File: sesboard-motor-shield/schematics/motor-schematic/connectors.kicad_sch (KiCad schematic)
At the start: 2 parts, among them J3 SESBOARD_1, J4 SESBOARD_2

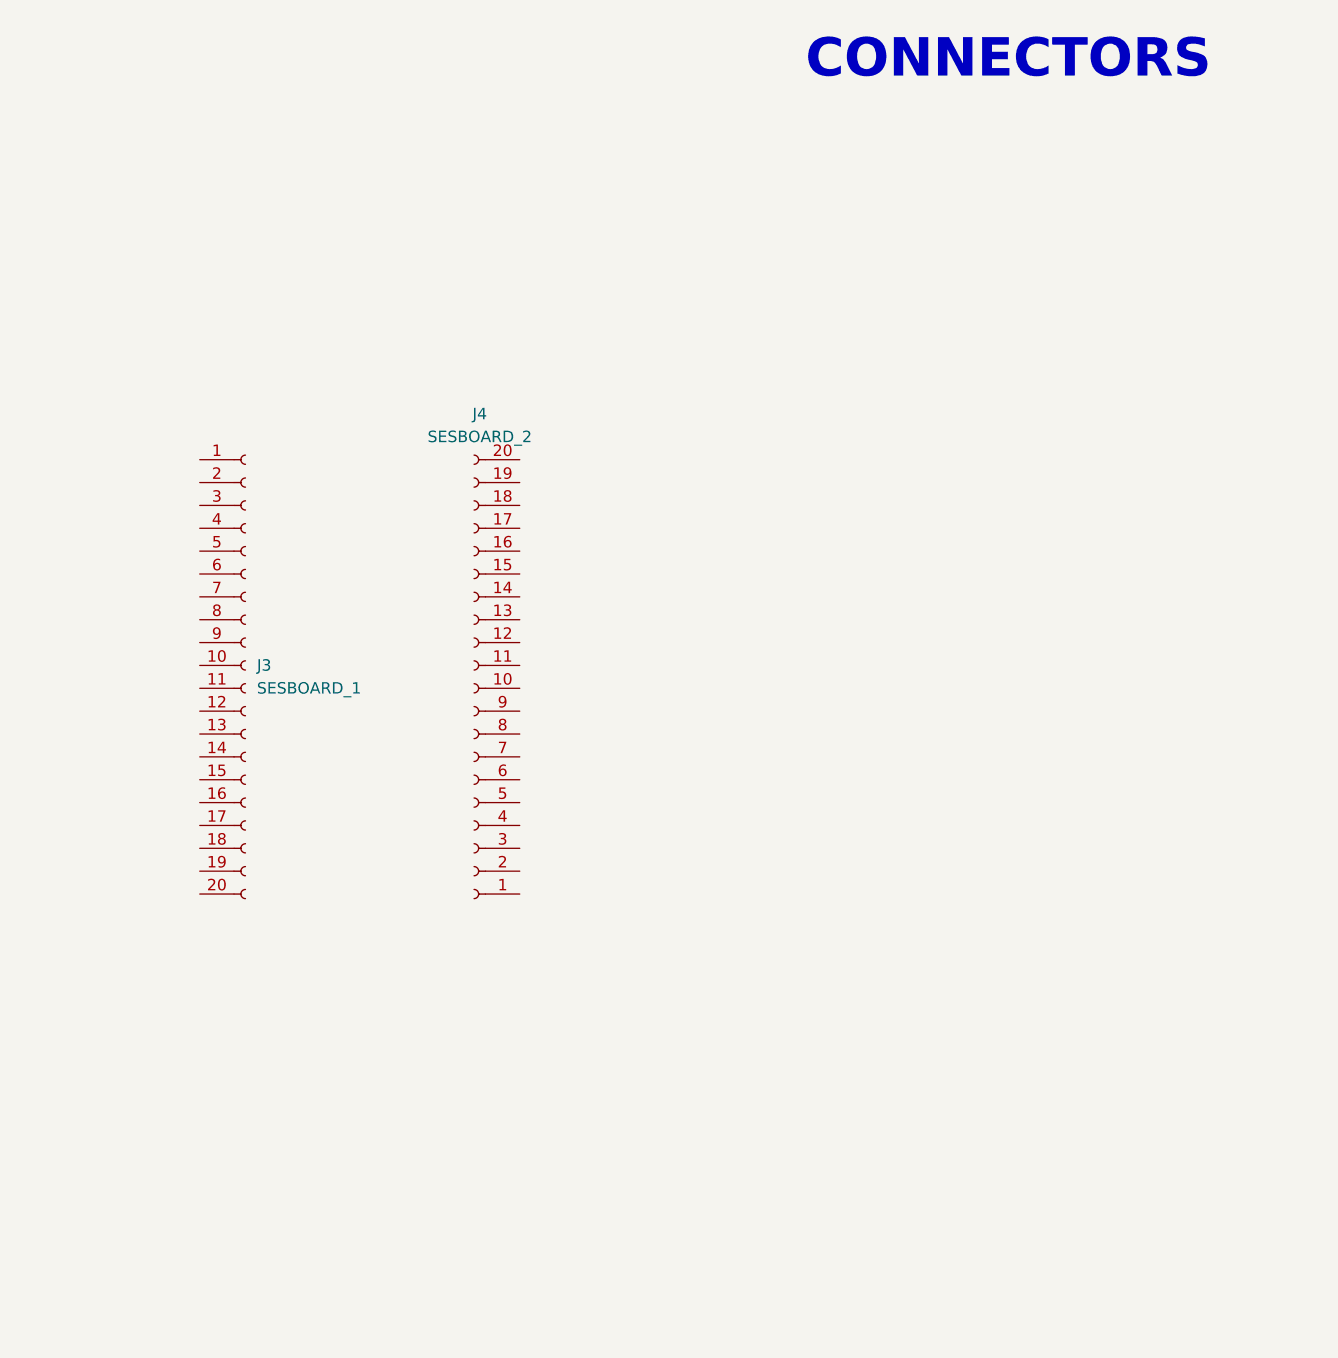
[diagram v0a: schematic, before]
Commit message: added stepper connector
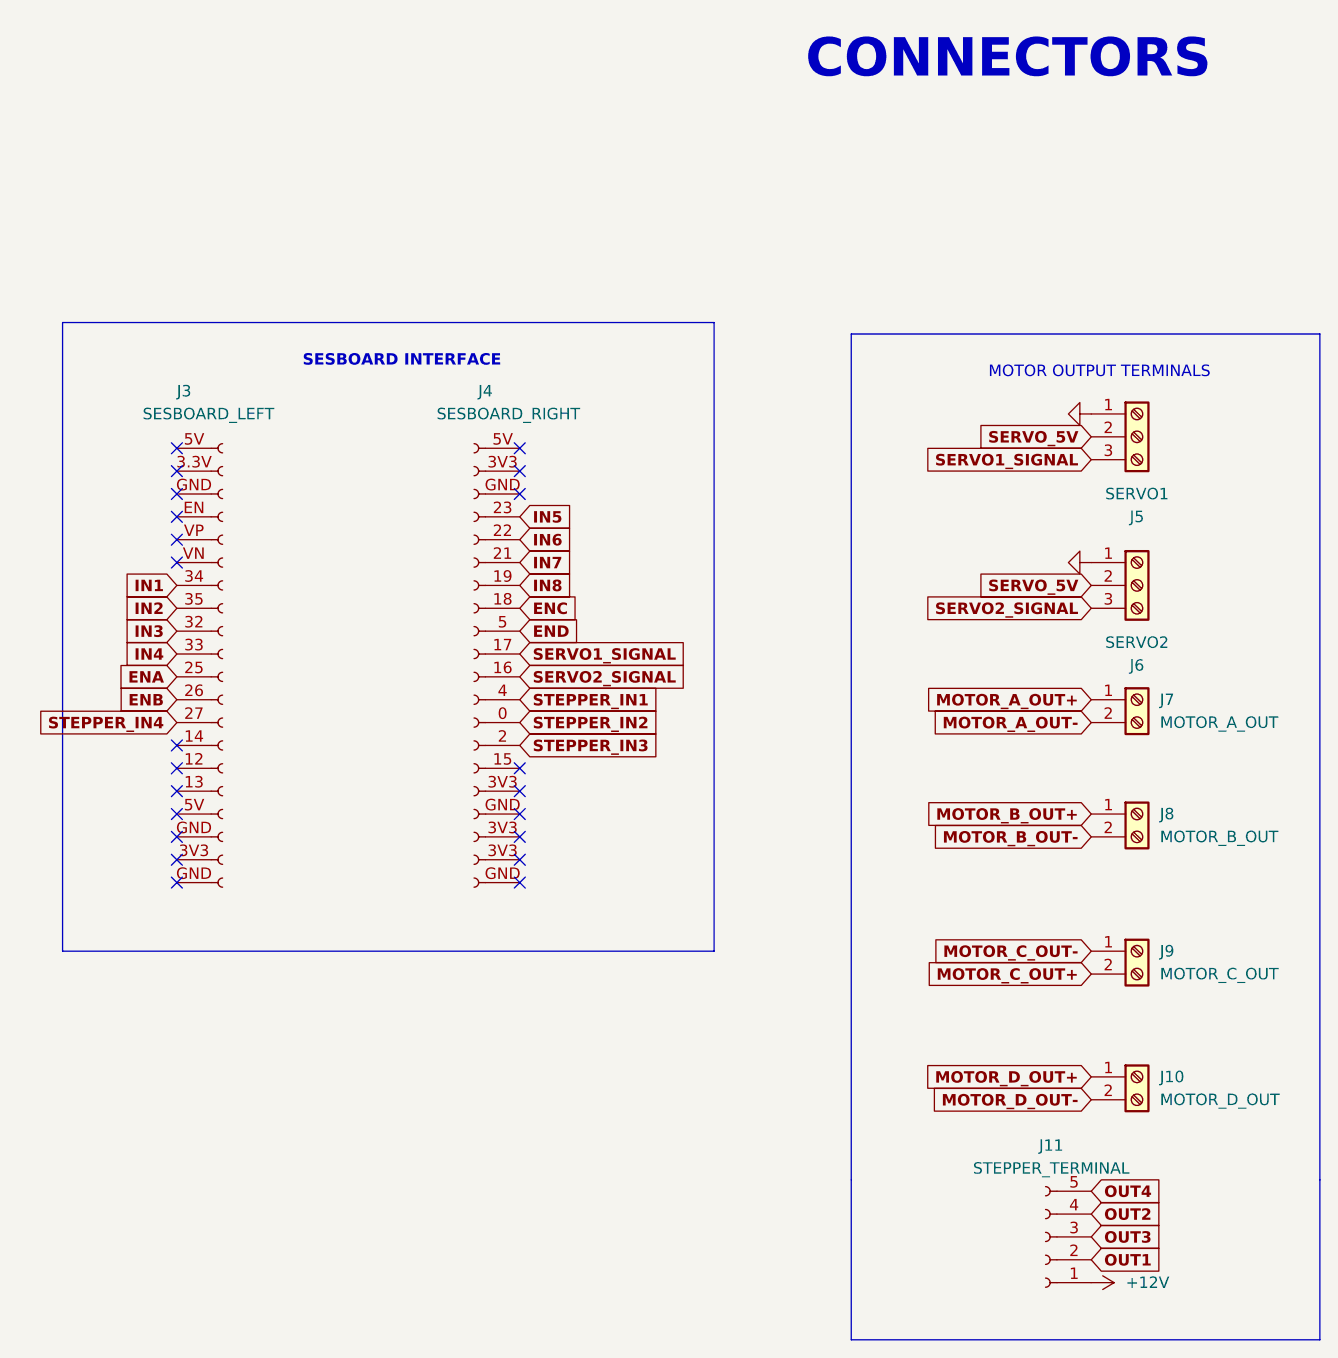
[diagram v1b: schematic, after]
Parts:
- added J10: MOTOR_D_OUT, TerminalBlock_Phoenix:TerminalBlock_Phoenix_MKDS-1,5-2_1x02_P5.00mm_Horizontal, symbol Connector:Screw_Terminal_01x02
- added J11: STEPPER_TERMINAL, Connector_PinHeader_2.54mm:PinHeader_1x05_P2.54mm_Vertical, symbol Connector:Conn_01x05_Female
- added J5: SERVO1, Connector_PinHeader_2.54mm:PinHeader_1x03_P2.54mm_Vertical, symbol Connector:Screw_Terminal_01x03
- added J6: SERVO2, Connector_PinHeader_2.54mm:PinHeader_1x03_P2.54mm_Vertical, symbol Connector:Screw_Terminal_01x03
- added J7: MOTOR_A_OUT, TerminalBlock_Phoenix:TerminalBlock_Phoenix_MKDS-1,5-2_1x02_P5.00mm_Horizontal, symbol Connector:Screw_Terminal_01x02
- added J8: MOTOR_B_OUT, TerminalBlock_Phoenix:TerminalBlock_Phoenix_MKDS-1,5-2_1x02_P5.00mm_Horizontal, symbol Connector:Screw_Terminal_01x02
- added J9: MOTOR_C_OUT, TerminalBlock_Phoenix:TerminalBlock_Phoenix_MKDS-1,5-2_1x02_P5.00mm_Horizontal, symbol Connector:Screw_Terminal_01x02
- J3: value SESBOARD_1 -> SESBOARD_LEFT
- J4: value SESBOARD_2 -> SESBOARD_RIGHT
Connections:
- net SERVO2_SIGNAL: now reaches J4.16 (11)
- net SERVO2_SIGNAL: now also J6.3 (Pin_3)
- net SERVO1_SIGNAL: now reaches J4.17 (10)
- net SERVO1_SIGNAL: now also J5.3 (Pin_3)
- net ENC: now reaches J4.18 (8)
- net IN8: now reaches J4.19 (7)
- net STEPPER_IN3: now reaches J4.2 (14)
- net STEPPER_IN1: now reaches J4.4 (12)
- net END: now reaches J4.5 (9)
- new net +12V: J11.1 (Pin_1)
- new net ENA: J3.25 (Pin_11)
- new net ENB: J3.26 (Pin_12)
- new net GND: J5.1 (Pin_1), J6.1 (Pin_1)
- new net IN1: J3.34 (7)
- new net IN2: J3.35 (8)
- new net IN3: J3.32 (9)
- new net IN4: J3.33 (Pin_10)
- new net IN5: J4.23 (4)
- new net IN6: J4.22 (5)
- new net IN7: J4.21 (6)
- new net MOTOR_A_OUT+: J7.1 (Pin_1)
- new net MOTOR_A_OUT-: J7.2 (Pin_2)
- new net MOTOR_B_OUT+: J8.1 (Pin_1)
- new net MOTOR_B_OUT-: J8.2 (Pin_2)
- new net MOTOR_C_OUT+: J9.2 (Pin_2)
- new net MOTOR_C_OUT-: J9.1 (Pin_1)
- new net MOTOR_D_OUT+: J10.1 (Pin_1)
- new net MOTOR_D_OUT-: J10.2 (Pin_2)
- new net OUT1: J11.2 (Pin_2)
- new net OUT2: J11.4 (Pin_4)
- new net OUT3: J11.3 (Pin_3)
- new net OUT4: J11.5 (Pin_5)
- new net SERVO_5V: J5.2 (Pin_2), J6.2 (Pin_2)
- new net STEPPER_IN2: J4.0 (13)
- new net STEPPER_IN4: J3.27 (Pin_13)
- no-connect marks 0 -> 22
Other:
- note added: "MOTOR OUTPUT TERMINALS"
- note added: "SESBOARD INTERFACE"
- moved on the sheet: J3

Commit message: added power toggle
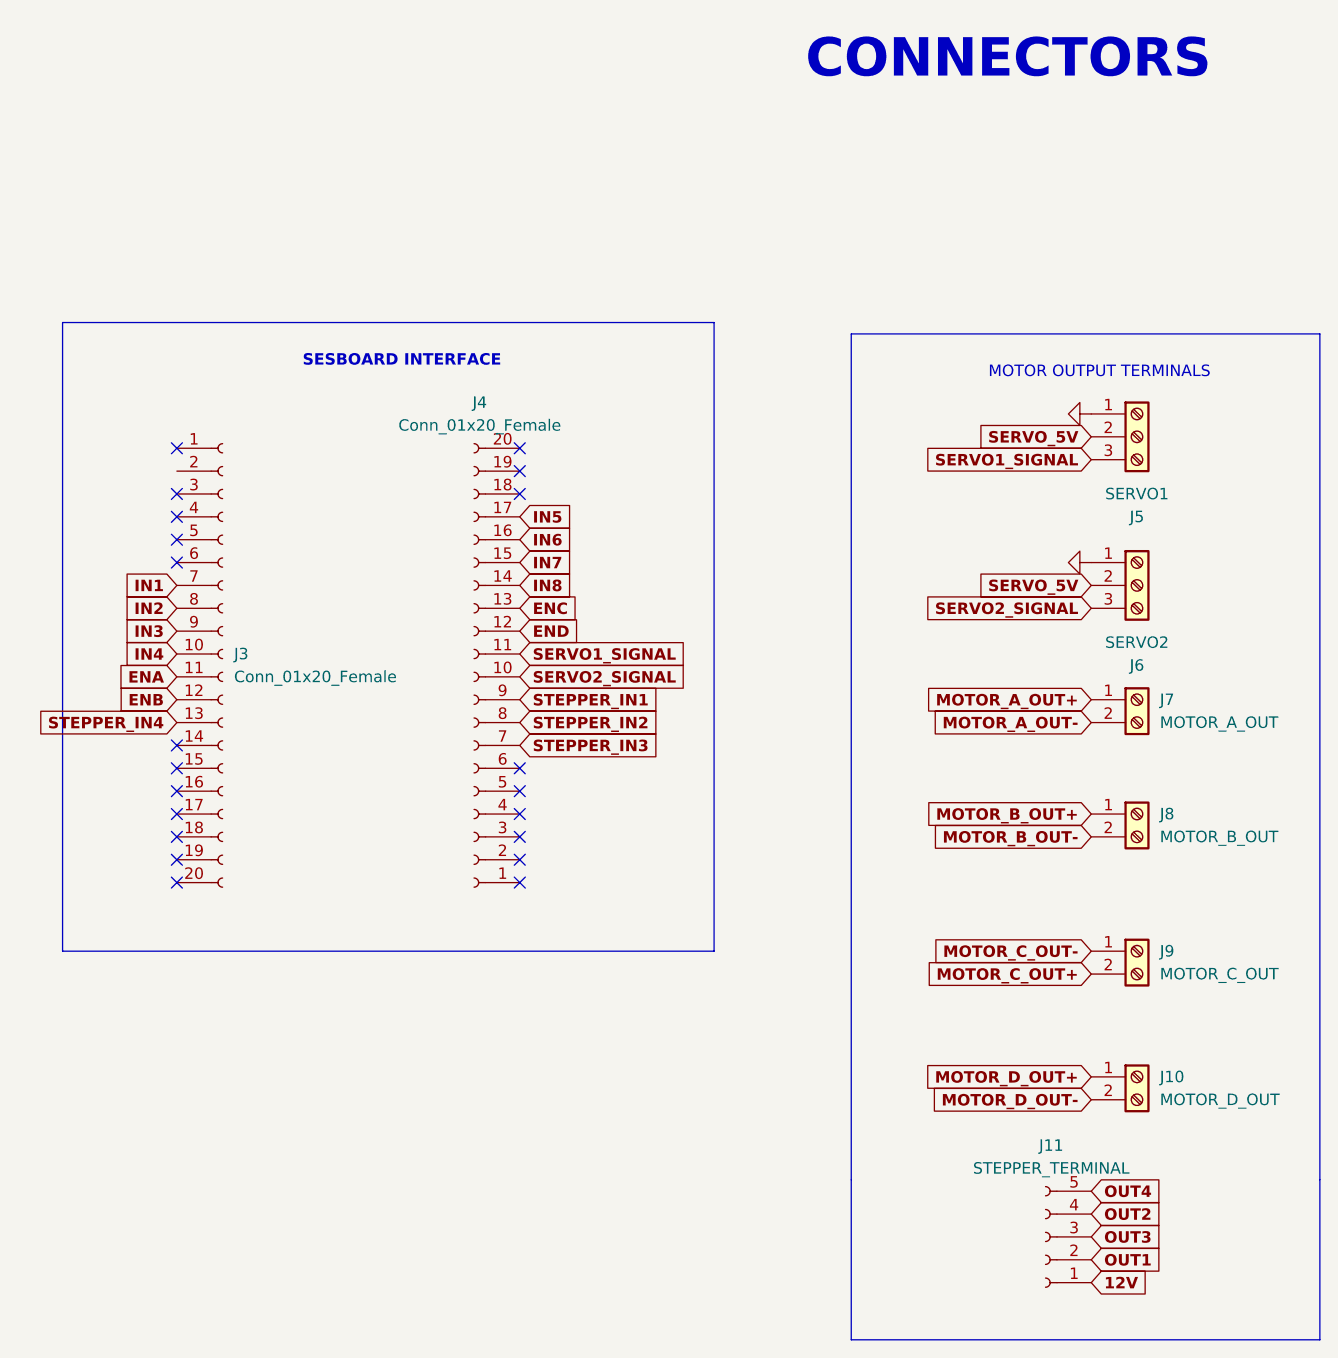
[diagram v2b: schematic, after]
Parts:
- J3: value SESBOARD_LEFT -> Conn_01x20_Female
- J4: value SESBOARD_RIGHT -> Conn_01x20_Female
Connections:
- net ENA: now also J3.11 (Pin_11); no longer J3.25 (Pin_11)
- net ENB: now also J3.12 (Pin_12); no longer J3.26 (Pin_12)
- net ENC: now also J4.13 (Pin_13); no longer J4.18 (8)
- net END: now also J4.12 (Pin_12); no longer J4.5 (9)
- net IN1: now also J3.7 (Pin_7); no longer J3.34 (7)
- net IN2: now also J3.8 (Pin_8); no longer J3.35 (8)
- net IN3: now also J3.9 (Pin_9); no longer J3.32 (9)
- net IN4: now also J3.10 (Pin_10); no longer J3.33 (Pin_10)
- net IN5: now also J4.17 (Pin_17); no longer J4.23 (4)
- net IN6: now also J4.16 (Pin_16); no longer J4.22 (5)
- net IN7: now also J4.15 (Pin_15); no longer J4.21 (6)
- net IN8: now also J4.14 (Pin_14); no longer J4.19 (7)
- net SERVO1_SIGNAL: now also J4.11 (Pin_11); no longer J4.17 (10)
- net SERVO2_SIGNAL: now also J4.10 (Pin_10); no longer J4.16 (11)
- net STEPPER_IN1: now also J4.9 (Pin_9); no longer J4.4 (12)
- net STEPPER_IN2: now also J4.8 (Pin_8); no longer J4.0 (13)
- net STEPPER_IN3: now also J4.7 (Pin_7); no longer J4.2 (14)
- net STEPPER_IN4: now also J3.13 (Pin_13); no longer J3.27 (Pin_13)
- net +12V renamed 12V
- no-connect marks 22 -> 21
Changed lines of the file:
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@@
 (kicad_sch (version 20211123) (generator eeschema)
   (paper "A4")
+  (no_connect (at 62.23 96.52))
+  (no_connect (at 62.23 99.06))
   (no_connect (at 62.23 101.6))
   (no_connect (at 100.33 99.06))
-  (no_connect (at 62.23 96.52))
-  (no_connect (at 62.23 99.06))
+  (no_connect (at 62.23 63.5))
+  (no_connect (at 62.23 73.66))
+  (no_connect (at 62.23 68.58))
+  (no_connect (at 62.23 71.12))
+  (no_connect (at 62.23 76.2))
   (no_connect (at 62.23 109.22))
   (no_connect (at 62.23 106.68))
-  (no_connect (at 100.33 101.6))
-  (no_connect (at 100.33 109.22))
-  (no_connect (at 100.33 111.76))
   (no_connect (at 62.23 104.14))
   (no_connect (at 62.23 111.76))
+  (no_connect (at 100.33 68.58))
+  (no_connect (at 100.33 66.04))
+  (no_connect (at 100.33 63.5))
+  (no_connect (at 100.33 111.76))
+  (no_connect (at 100.33 109.22))
+  (no_connect (at 100.33 101.6))
+  (no_connect (at 100.33 106.68))
   (no_connect (at 100.33 104.14))
-  (no_connect (at 100.33 106.68))
-  (no_connect (at 100.33 66.04))
-  (no_connect (at 100.33 68.58))
-  (no_connect (at 100.33 63.5))
-  (no_connect (at 62.23 63.5))
-  (no_connect (at 62.23 66.04))
-  (no_connect (at 62.23 68.58))
-  (no_connect (at 62.23 71.12))
-  (no_connect (at 62.23 73.66))
-  (no_connect (at 62.23 76.2))
   (polyline (pts (xy 189.23 162.56) (xy 189.23 144.78))
     (stroke (width 0) (type default) (color 0 0 0 0))
@@
     )
   )
+  (global_label "12V" (shape input) (at 163.83 156.21 0) (fields_autoplaced)
+    (effects (font (size 1.27 1.27) bold) (justify left))
+    (property "Intersheet References" "${INTERSHEET_REFS}" (id 0) (at 169.9411 156.083 0)
+      (effects (font (size 1.27 1.27) bold) (justify left) hide)
+    )
+  )
   (global_label "END" (shape input) (at 100.33 83.82 0) (fields_autoplaced)
     (effects (font (size 1.27 1.27) bold) (justify left))
@@
     )
   )
-  (symbol (lib_id "Connector:Screw_Terminal_01x02") (at 168.91 119.38 0) (unit 1)
-    (in_bom yes) (on_board yes) (fields_autoplaced)
-    (property "Reference" "J9" (id 0) (at 171.45 119.3799 0)
-      (effects (font (size 1.27 1.27)) (justify left))
-    )
-    (property "Value" "MOTOR_C_OUT" (id 1) (at 171.45 121.9199 0)
-      (effects (font (size 1.27 1.27)) (justify left))
-    )
-    (property "Footprint" "TerminalBlock_Phoenix:TerminalBlock_Phoenix_MKDS-1,5-2_1x02_P5.00mm_Horizontal" (id 2) (at 168.91 119.38 0)
-      (effects (font (size 1.27 1.27)) hide)
-    )
-    (property "Datasheet" "~" (id 3) (at 168.91 119.38 0)
-      (effects (font (size 1.27 1.27)) hide)
-    )
-    (pin "1")
-    (pin "2")
-  )
-  (symbol (lib_id "power:+12V") (at 163.83 156.21 270) (unit 1)
-    (in_bom yes) (on_board yes) (fields_autoplaced)
-    (property "Reference" "#PWR026" (id 0) (at 160.02 156.21 0)
-      (effects (font (size 1.27 1.27)) hide)
-    )
-    (property "Value" "+12V" (id 1) (at 167.64 156.2099 90)
-      (effects (font (size 1.27 1.27)) (justify left))
-    )
-    (property "Footprint" "" (id 2) (at 163.83 156.21 0)
-      (effects (font (size 1.27 1.27)) hide)
-    )
-    (property "Datasheet" "" (id 3) (at 163.83 156.21 0)
-      (effects (font (size 1.27 1.27)) hide)
-    )
-    (pin "1")
-  )
-  (symbol (lib_id "Connector:Conn_01x20_Female") (at 93.98 93.98 0) (unit 1)
-    (in_bom yes) (on_board yes)
-    (property "Reference" "J4" (id 0) (at 96.52 57.15 0))
-    (property "Value" "SESBOARD_RIGHT" (id 1) (at 99.06 59.69 0))
-    (property "Footprint" "Connector_PinHeader_2.54mm:PinHeader_1x20_P2.54mm_Vertical" (id 2) (at 95.25 88.9 0)
-      (effects (font (size 1.27 1.27)) hide)
-    )
-    (property "Datasheet" "~" (id 3) (at 95.25 88.9 0)
-      (effects (font (size 1.27 1.27)) hide)
-    )
-    (pin "0")
+  (symbol (lib_id "Connector:Conn_01x20_Female") (at 67.31 86.36 0) (unit 1)
+    (in_bom yes) (on_board yes) (fields_autoplaced)
+    (property "Reference" "J3" (id 0) (at 68.58 86.3599 0)
+      (effects (font (size 1.27 1.27)) (justify left))
+    )
+    (property "Value" "Conn_01x20_Female" (id 1) (at 68.58 88.8999 0)
+      (effects (font (size 1.27 1.27)) (justify left))
+    )
+    (property "Footprint" "Connector_PinHeader_2.54mm:PinHeader_1x20_P2.54mm_Vertical" (id 2) (at 67.31 86.36 0)
+      (effects (font (size 1.27 1.27)) hide)
+    )
+    (property "Datasheet" "~" (id 3) (at 67.31 86.36 0)
+      (effects (font (size 1.27 1.27)) hide)
+    )
+    (pin "1")
+    (pin "10")
+    (pin "11")
+    (pin "12")
+    (pin "13")
+    (pin "14")
     (pin "15")
     (pin "16")
@@
     (pin "19")
     (pin "2")
-    (pin "21")
-    (pin "22")
-    (pin "23")
-    (pin "3V3")
-    (pin "3V3")
-    (pin "3V3")
-    (pin "3V3")
+    (pin "20")
+    (pin "3")
     (pin "4")
     (pin "5")
-    (pin "5V")
-    (pin "GND")
-    (pin "GND")
-    (pin "GND")
-  )
-  (symbol (lib_name "Conn_01x20_Female_1") (lib_id "Connector:Conn_01x20_Female") (at 67.31 86.36 0) (unit 1)
-    (in_bom yes) (on_board yes)
-    (property "Reference" "J3" (id 0) (at 62.23 57.15 0)
-      (effects (font (size 1.27 1.27)) (justify left))
-    )
-    (property "Value" "SESBOARD_LEFT" (id 1) (at 58.42 59.69 0)
-      (effects (font (size 1.27 1.27)) (justify left))
-    )
-    (property "Footprint" "Connector_PinHeader_2.54mm:PinHeader_1x20_P2.54mm_Vertical" (id 2) (at 67.31 73.66 0)
-      (effects (font (size 1.27 1.27)) hide)
-    )
-    (property "Datasheet" "~" (id 3) (at 67.31 86.36 0)
-      (effects (font (size 1.27 1.27)) hide)
-    )
-    (pin "5V")
-    (pin "33")
-    (pin "25")
-    (pin "26")
-    (pin "27")
-    (pin "14")
-    (pin "12")
-    (pin "13")
-    (pin "5V")
-    (pin "GND")
-    (pin "3V3")
-    (pin "3.3V")
-    (pin "GND")
-    (pin "GND")
-    (pin "EN")
-    (pin "VP")
-    (pin "VN")
-    (pin "34")
-    (pin "35")
-    (pin "32")
+    (pin "6")
+    (pin "7")
+    (pin "8")
+    (pin "9")
+  )
+  (symbol (lib_id "Connector:Screw_Terminal_01x02") (at 168.91 119.38 0) (unit 1)
+    (in_bom yes) (on_board yes) (fields_autoplaced)
+    (property "Reference" "J9" (id 0) (at 171.45 119.3799 0)
+      (effects (font (size 1.27 1.27)) (justify left))
+    )
+    (property "Value" "MOTOR_C_OUT" (id 1) (at 171.45 121.9199 0)
+      (effects (font (size 1.27 1.27)) (justify left))
+    )
+    (property "Footprint" "TerminalBlock_Phoenix:TerminalBlock_Phoenix_MKDS-1,5-2_1x02_P5.00mm_Horizontal" (id 2) (at 168.91 119.38 0)
+      (effects (font (size 1.27 1.27)) hide)
+    )
+    (property "Datasheet" "~" (id 3) (at 168.91 119.38 0)
+      (effects (font (size 1.27 1.27)) hide)
+    )
+    (pin "1")
+    (pin "2")
   )
   (symbol (lib_id "power:GND") (at 163.83 59.69 270) (unit 1)
@@
     (pin "3")
   )
+  (symbol (lib_id "Connector:Conn_01x20_Female") (at 95.25 88.9 180) (unit 1)
+    (in_bom yes) (on_board yes) (fields_autoplaced)
+    (property "Reference" "J4" (id 0) (at 95.885 58.42 0))
+    (property "Value" "Conn_01x20_Female" (id 1) (at 95.885 60.96 0))
+    (property "Footprint" "Connector_PinHeader_2.54mm:PinHeader_1x20_P2.54mm_Vertical" (id 2) (at 95.25 88.9 0)
+      (effects (font (size 1.27 1.27)) hide)
+    )
+    (property "Datasheet" "~" (id 3) (at 95.25 88.9 0)
+      (effects (font (size 1.27 1.27)) hide)
+    )
+    (pin "1")
+    (pin "10")
+    (pin "11")
+    (pin "12")
+    (pin "13")
+    (pin "14")
+    (pin "15")
+    (pin "16")
+    (pin "17")
+    (pin "18")
+    (pin "19")
+    (pin "2")
+    (pin "20")
+    (pin "3")
+    (pin "4")
+    (pin "5")
+    (pin "6")
+    (pin "7")
+    (pin "8")
+    (pin "9")
+  )
   (symbol (lib_id "Connector:Screw_Terminal_01x02") (at 168.91 104.14 0) (unit 1)
